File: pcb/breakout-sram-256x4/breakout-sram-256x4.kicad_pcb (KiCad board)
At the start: 6 copper layers, 100 x 51.2 mm, 34 parts, among them J1 DF40C-100DS-0.4V51, J10 DF40C-40DP-0.4V51, J2 DF40C-100DS-0.4V51, J3 DF40C-100DS-0.4V51, J4 DF40C-100DS-0.4V51, J5 DF40C-100DP-0.4V51, J6 DF40C-100DP-0.4V51, J7 DF40C-100DP-0.4V51, J8 DF40C-100DP-0.4V51, J9 DF40C-40DS-0.4V51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

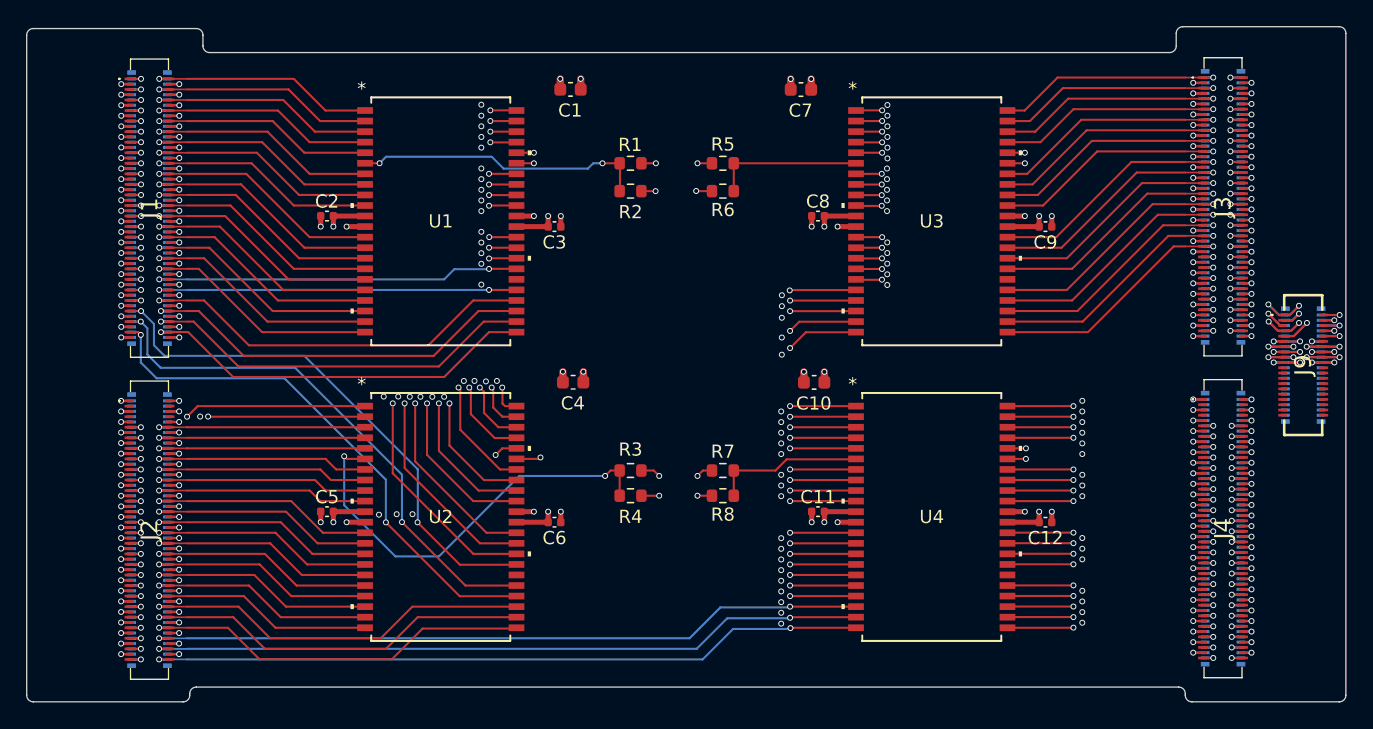
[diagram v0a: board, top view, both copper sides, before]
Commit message: [sram_4x][pcb] pull in traces and edge cut for more clearance
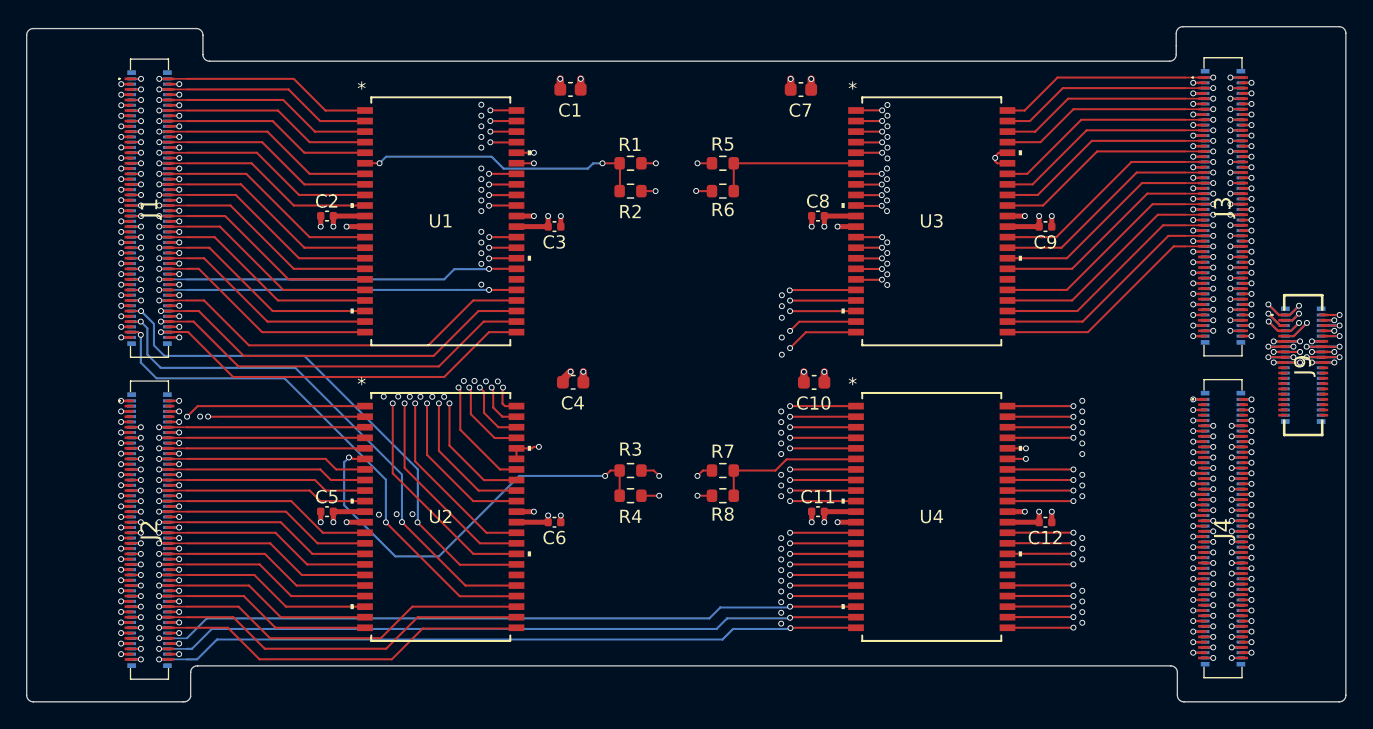
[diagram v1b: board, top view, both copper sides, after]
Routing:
- net B_55: track 60.5 -> 58.8 mm
- net B_43: track 60.5 -> 58.8 mm
- net B_59: track 60.2 -> 58.5 mm
- net B_51: track 60.6 -> 58.8 mm
- net B_47: track 60.5 -> 58.8 mm
- net B_91: track 59.5 -> 57.8 mm
- net B_75: track 59.5 -> 57.8 mm
- net B_71: track 60.1 -> 58.5 mm
- net B_67: track 60.1 -> 58.5 mm
- net B_95: track 59.5 -> 57.8 mm
- net B_83: track 59.5 -> 57.8 mm
- net B_87: track 59.5 -> 57.8 mm
- net B_63: track 60.1 -> 58.5 mm
- net B_79: track 59.5 -> 57.8 mm
- net B_99: track 59.5 -> 57.8 mm
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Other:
- outline, holes or cut-outs redrawn

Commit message: [hx8k][pcb] define 8 layer stackup
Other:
- copper layers 6 -> 8
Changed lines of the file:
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@@
 		(8 "In3.Cu" signal)
 		(10 "In4.Cu" power)
+		(12 "In5.Cu" signal)
+		(14 "In6.Cu" signal)
 		(2 "B.Cu" signal)
 		(9 "F.Adhes" user "F.Adhesive")
@@
 			(layer "dielectric 2"
 				(type "core")
-				(thickness 0.535)
+				(thickness 0.3)
 				(material "FR4")
 				(epsilon_r 4.5)
@@
 			(layer "dielectric 4"
 				(type "core")
-				(thickness 0.535)
+				(thickness 0.3)
 				(material "FR4")
 				(epsilon_r 4.5)
@@
 				(type "prepreg")
 				(thickness 0.1)
+				(material "FR4")
+				(epsilon_r 4.5)
+				(loss_tangent 0.02)
+			)
+			(layer "In5.Cu"
+				(type "copper")
+				(thickness 0.035)
+			)
+			(layer "dielectric 6"
+				(type "core")
+				(thickness 0.3)
+				(material "FR4")
+				(epsilon_r 4.5)
+				(loss_tangent 0.02)
+			)
+			(layer "In6.Cu"
+				(type "copper")
+				(thickness 0.035)
+			)
+			(layer "dielectric 7"
+				(type "prepreg")
+				(thickness 0.1)
